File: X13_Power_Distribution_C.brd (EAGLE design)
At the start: 152.4 x 73.7 mm, 42 parts, among them Q1 IRF1018EPBF, Q2 SSM3K341R, Q3 IRF1018EPBF, Q4 IRF1018EPBF, Q5 SSM3K341R, Q6 SSM3K341R

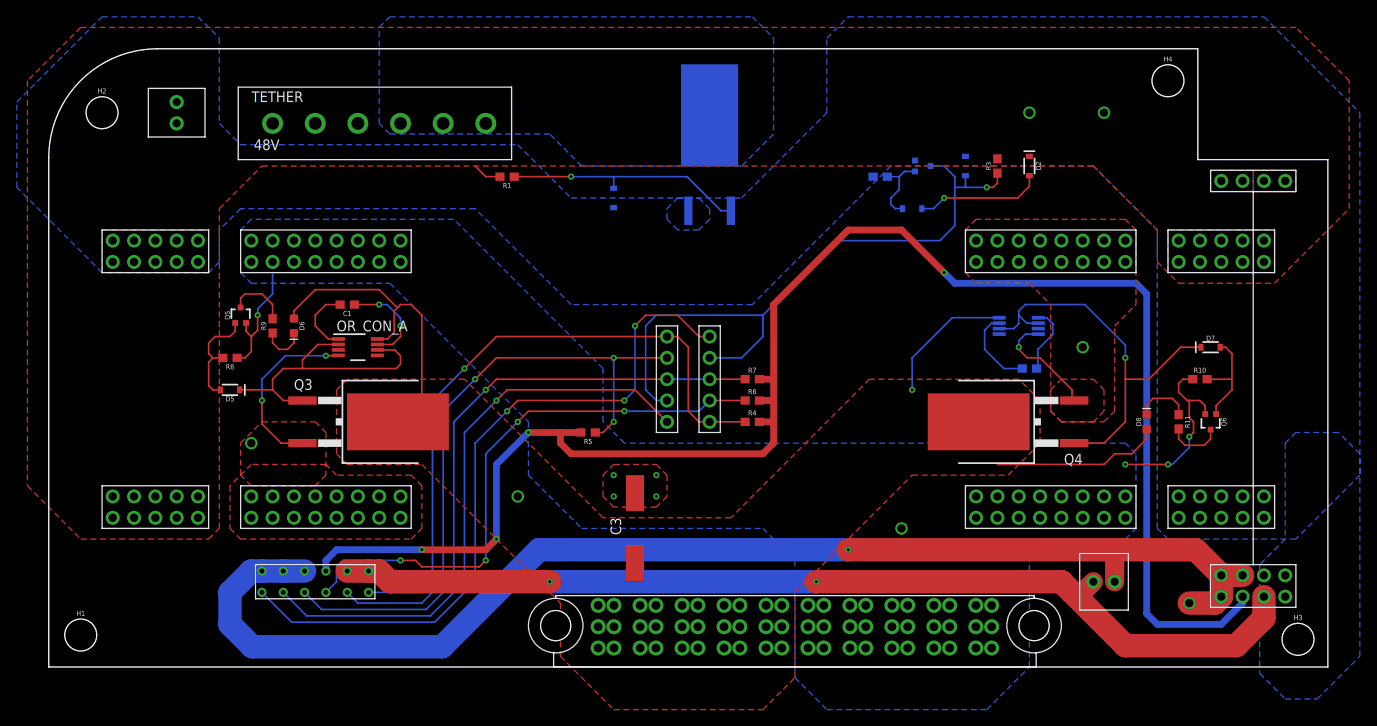
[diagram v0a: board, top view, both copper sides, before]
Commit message: Added LM5050, tweaks
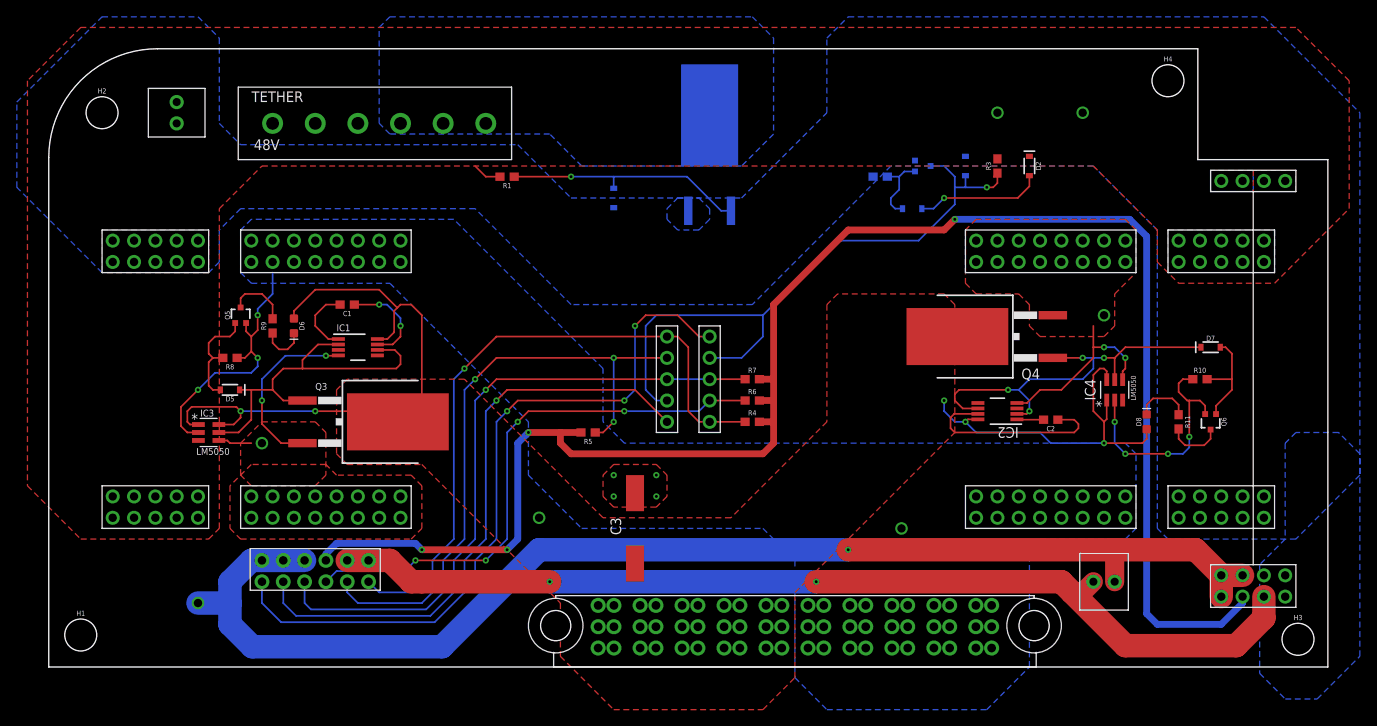
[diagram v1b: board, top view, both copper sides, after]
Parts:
- removed OR_CON_B: (no value), Dist_OR_Controller:DGK0008A_M
- added IC2: LM74610, Dist_OR_Controller:DGK0008A_M
- added IC3, IC4: LM5050, Dist_OR_Controller:MK06A-M
- BACKPLANE_LOGIC: value IPL1-107-01-L-D-RE-P -> IPL1-106-01-L-D-RE1-K; device Backplane_Dist_Logic_Connector:IPL1-107-01-L-D-RE-P -> Backplane_Dist_Logic_Connector:IPL1-106-01-L-D-RE1-K
- IC1: value (none) -> LM74610
- moved Q4 10.5 mm to (113.0, 39.4)
- moved C2 6.60 mm to (119.4, 29.5), flipped to the top
- moved BACKPLANE_LOGIC 1.27 mm to (25.4, 12.7)
- renumbered OR_CON_A to IC1
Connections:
- net +12V: now also IC2.8, IC3.1, IC3.6, IC4.1, IC4.6; no longer OR_CON_B.8
- net +12V_A: now also IC3.4
- net +12V_B: now also IC2.4, IC4.4; no longer OR_CON_B.4
- net 12V_GND: now also IC3.2, IC4.2
- net OR_DRIVE_A: now also IC3.5
- net OR_DRIVE_B: now also IC2.2, IC2.6, IC4.5; no longer OR_CON_B.2, OR_CON_B.6
- net VCAPH_B: now also IC2.7; no longer OR_CON_B.7
- net VCAPL_B: now also IC2.1; no longer OR_CON_B.1
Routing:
- net +12V: track 76.0 -> 111.2 mm, vias 2 -> 6
- net 12V_GND: track 36.5 -> 60.4 mm, vias 9 -> 12
- net VCAPH_B: track 9.80 -> 23.5 mm
- net +12V_B: track 13.4 -> 22.2 mm, vias 2 -> 3
- net OR_DRIVE_A: track 35.4 -> 43.4 mm
- net +3.3V: track 195.6 -> 202.0 mm
- net VCAPL_B: track 8.18 -> 3.19 mm
- net +12V_A: track 21.4 -> 25.4 mm
- net ALERT_2: track 68.5 -> 66.3 mm
- net C2_2: track 85.2 -> 87.2 mm
- net CLK: track 75.9 -> 77.9 mm
- net C2_1: track 70.0 -> 72.0 mm
- net ON/OFF: track 80.1 -> 78.6 mm
- net ALERT_1: track 73.0 -> 74.2 mm
- net +5V: track 152.0 -> 153.0 mm
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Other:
- board text added: "48V_ETHERNET"
- board text added: "5V_ETHERNET"
- board text added: "LM74610"

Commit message: More tweaks
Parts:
- moved R7 2.54 mm to (83.8, 36.8)
- moved R6 1.27 mm to (83.8, 33.0)
- renumbered IC1 to U1, IC2 to U2, IC3 to U3, IC4 to U4
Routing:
- net CLK: track 77.9 -> 78.9 mm
- net ALERT_2: track 66.3 -> 66.9 mm
